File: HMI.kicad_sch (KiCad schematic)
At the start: 1 part, among them U8 XIAO-RP2350-SMD

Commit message: many changes
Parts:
- added C12, C40, C41, C42, C43, C44: 470n, Capacitor_SMD:C_1210_3225Metric_Pad1.33x2.70mm_HandSolder, symbol Device:C
- added C15, C16, C19, C20, C21, C22, C25, C26: 100n, Capacitor_SMD:C_1210_3225Metric_Pad1.33x2.70mm_HandSolder, symbol Device:C
- added C23, C24: 22p, Capacitor_SMD:C_1210_3225Metric_Pad1.33x2.70mm_HandSolder, symbol Device:C
- added D21, D22: LED, LED_SMD:LED_1210_3225Metric_Pad1.42x2.65mm_HandSolder, symbol Device:LED
- added J2: Conn_01x04, I2C OLED:I2C OLED, symbol Connector_Generic:Conn_01x04
- added J3: Conn_01x06, Connector_JST:JST_PH_B6B-PH-K_1x06_P2.00mm_Vertical, symbol Connector_Generic:Conn_01x06
- added LED1, LED2, LED3, LED4, LED5, LED6: SK6812MINI-E, PCM_marbastlib-various:LED_6028R, symbol PCM_marbastlib-various:SK6812MINI-E
- added MX1, MX2, MX3, MX4, MX5, MX6: MX_SW_solder, PCM_marbastlib-mx:SW_MX_1u, symbol PCM_marbastlib-mx:MX_SW_solder
- added R16, R17, R18, R23, R24, R25, R26, R27, R28, R29, R30, R31, R32, R33, R34, R35, R36, R37, R44, R8, R9: 10k, Resistor_SMD:R_1210_3225Metric_Pad1.30x2.65mm_HandSolder, symbol Device:R
- added R38, R39: 5.1k, Resistor_SMD:R_1210_3225Metric_Pad1.30x2.65mm_HandSolder, symbol Device:R
- added R40, R41, R42, R43, R45: 330, Resistor_SMD:R_1210_3225Metric_Pad1.30x2.65mm_HandSolder, symbol Device:R
- added RV4, RV5, RV6, RV7: 10k, Potentiometer_THT:Potentiometer_Bourns_3299W_Vertical, symbol Device:R_Potentiometer_Trim
- added SW1, SW2: RotaryEncoder_Switch, Rotary_Encoder:RotaryEncoder_Alps_EC11E-Switch_Vertical_H20mm, symbol Device:RotaryEncoder_Switch
- added TP4: SDA0, TestPoint:TestPoint_Keystone_5019_Miniature, symbol Connector:TestPoint
- added TP5: SCL0, TestPoint:TestPoint_Keystone_5019_Miniature, symbol Connector:TestPoint
- added TP6: SDA1, TestPoint:TestPoint_Keystone_5019_Miniature, symbol Connector:TestPoint
- added TP7: SCL1, TestPoint:TestPoint_Keystone_5019_Miniature, symbol Connector:TestPoint
- added U10: 74AHC1G14, symbol 74xGxx:74AHC1G14
- added U11: CH340G, Package_SO:SOIC-16_3.9x9.9mm_P1.27mm, symbol Interface_USB:CH340G
- added U12, U9: Optocoupler_DC_PhotoNPN_AKEC, Package_DIP:DIP-4_W7.62mm_Socket_LongPads, symbol Isolator:Optocoupler_DC_PhotoNPN_AKEC
- added U6: MCP23018x-x-SO, Package_SO:SOIC-28W_7.5x17.9mm_P1.27mm, symbol Interface_Expansion:MCP23018x-x-SO
- added Y1: 12MHz, Crystal:Crystal_SMD_3225-4Pin_3.2x2.5mm, symbol Device:Crystal_GND24
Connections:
- net +5V: now also U10.5 (VCC)
- net GND: now also C12.2, C15.2, C16.2, C19.2, C20.2, C21.2, C22.2, C40.2, C41.2, C42.2, C43.2, C44.2, J2.1 (Pin_1), LED1.4 (VSS), LED2.4 (VSS), LED3.4 (VSS), LED4.4 (VSS), LED5.4 (VSS), LED6.4 (VSS), R9.1, SW1.C, SW1.S2, SW2.C, SW2.S2, U10.3 (GND), U12.2, U6.1 (V_{SS}), U9.3
- net CV_{thermal}: now reaches U8.1 (GPIO26/D0/ADC0)
- net OE: now reaches U8.10 (GPIO4/D9/SPI0_MISO)
- net SPI: now reaches U8.11 (GPIO3/D10/SPI0_MOSI)
- net SPI: now also R45.1
- net +3V3: now reaches U8.12 (3V3)
- net +3V3: now also MX1.1, MX2.1, MX3.1, MX4.1, MX5.1, MX6.1, R18.2, R23.2, R24.2, R28.2, R29.2, R30.2, R44.2, R8.1, RV4.2, RV4.3, RV5.2, RV5.3, RV6.2, RV6.3, RV7.2, RV7.3, U6.11 (V_{DD})
- net RXD: now reaches U8.15 (GPIO21/D11/RX1)
- net RXD: now also R41.1, R44.1
- net TXD: now reaches U8.16 (GPIO20/D12/TX1)
- net TXD: now also R40.1
- net CC_{thermal}: now reaches U8.2 (GPIO27/D1/ADC1)
- net SDA1: now reaches U8.5 (GPIO6/D4/SDA1)
- net SDA1: now also J2.4 (Pin_4), RV6.1, TP6.1, U6.13 (SDA)
- net SCL1: now reaches U8.6 (GPIO7/D5/SCL1)
- net SCL1: now also J2.3 (Pin_3), RV7.1, TP7.1, U6.12 (SCL)
- net muxIntA: now reaches U8.8 (GPIO1/D7/RX0)
- net muxIntA: now also U6.19 (INTA)
- net muxIntB: now reaches U8.9 (GPIO2/D8/SPI0_SCK)
- net muxIntB: now also U6.18 (INTB)
- net SCL renamed SCL0
- net SCL0: now also RV5.1, TP5.1
- net SDA renamed SDA0
- net SDA0: now also RV4.1, TP4.1
- new net: MX1.2, R32.1
- new net: MX2.2, R33.1
- new net: R16.2, R23.1, SW1.B
- new net: MX6.2, R37.1
- new net: D22.1 (K), U12.4
- new net: LED2.2 (DOUT), LED3.3 (DIN)
- new net: LED1.2 (DOUT), LED2.3 (DIN)
- new net: R26.2, R28.1, SW2.A
- new net: R30.1, R31.1, SW2.S1
- new net: LED5.2 (DOUT), LED6.3 (DIN)
- new net: LED4.2 (DOUT), LED5.3 (DIN)
- new net: LED1.3 (DIN), U10.4
- new net: R27.2, R29.1, SW2.B
- new net: R17.2, R18.1, SW1.A
- new net: C25.1, U11.4 (V3)
- new net: MX3.2, R34.1
- new net: R24.1, R25.1, SW1.S1
- new net: MX4.2, R35.1
- new net: R9.2, U6.15 (ADDR)
- new net: R8.2, U6.16 (~{RESET})
- new net: MX5.2, R36.1
- new net: R41.2, U9.4
- new net: R45.2, U10.2
- new net: D21.1 (K), U9.1
- new net: R43.1, U9.2
- new net: LED3.2 (DOUT), LED4.3 (DIN)
- new net: R43.2, U11.2 (TXD)
- new net: R42.2, U11.3 (RXD)
- new net: C23.2, U11.7 (XI), Y1.3
- new net: C24.2, U11.8 (XO), Y1.1
- new net: R40.2, U12.1
- new net: R42.1, U12.3
- new net CC1: J3.2 (Pin_2), R39.2
- new net CC2: J3.3 (Pin_3), R38.2
- new net GNDD: C23.1, C24.1, C25.2, C26.2, J3.6 (Pin_6), R38.1, R39.1, U11.1 (GND), Y1.2 (G), Y1.4 (G)
- new net UD+: J3.4 (Pin_4), U11.5 (UD+)
- new net UD-: J3.5 (Pin_5), U11.6 (UD-)
- new net VUSB: C26.1, D21.2 (A), D22.2 (A), J3.1 (Pin_1), U11.16 (VCC)
- new net V_{OUT}+5V: J2.2 (Pin_2), LED1.1 (VDD), LED2.1 (VDD), LED3.1 (VDD), LED4.1 (VDD), LED5.1 (VDD), LED6.1 (VDD)
- new net btnCC: C41.1, R36.2, U6.7 (GPB4)
- new net btnCV: C12.1, R35.2, U6.6 (GPB3)
- new net btnCancel: C42.1, R32.2, U6.3 (GPB0)
- new net btnI_{lim}: C43.1, R34.2, U6.5 (GPB2)
- new net btnOE: C44.1, R37.2, U6.8 (GPB5)
- new net btnV_{lim}: C40.1, R33.2, U6.4 (GPB1)
- new net encLimA: C20.1, R26.1, U6.23 (GPA3)
- new net encLimB: C21.1, R27.1, U6.24 (GPA4)
- new net encLimS: C22.1, R31.2, U6.25 (GPA5)
- new net encSetA: C16.1, R17.1, U6.20 (GPA0)
- new net encSetB: C15.1, R16.1, U6.21 (GPA1)
- new net encSetS: C19.1, R25.2, U6.22 (GPA2)
- no-connect marks 0 -> 26
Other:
- note added: "12.345"
- note added: "CV"
- note added: "ENC_{lim}"
- note added: "ENC_{set}"
- note added: "GPIO expander"
- note added: "I2C0 for PSU monitoring + control"
- note added: "I2C1 for HMI"
- note added: "Key backlighting"
- note added: "Meas 12.345 A"
- note added: "Rotary encoders + debouncing"
- note added: "SP 12.345 V"
- note added: "To I2C Display"
- note added: "USB -> UART + optical isolation"
- note added: "btn CV btn CC"
- note added: "btn Cancel"
- note added: "btn I_{lim}"
- note added: "btn OE"
- note added: "btn V_{lim}"
- moved on the sheet: U8

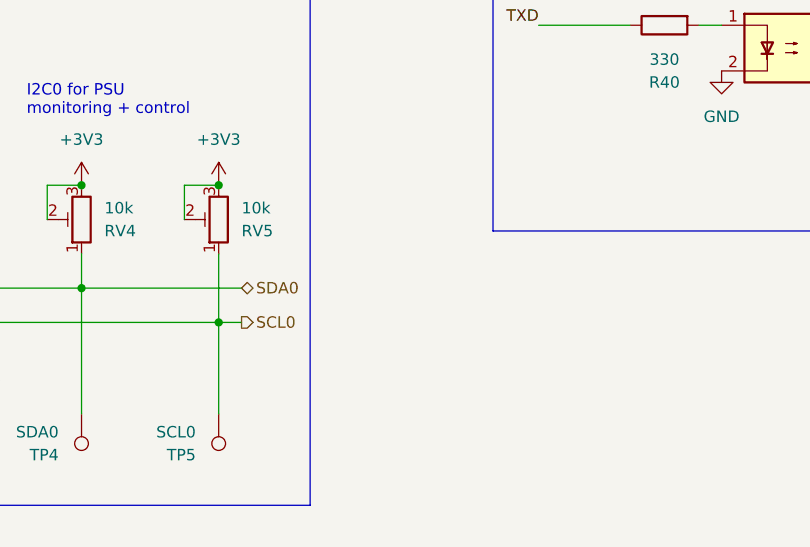
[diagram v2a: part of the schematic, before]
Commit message: shrink regulator board a little
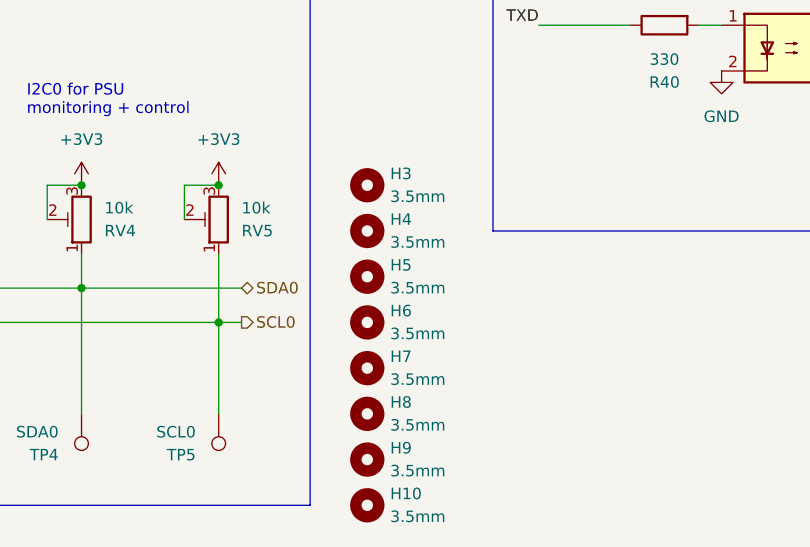
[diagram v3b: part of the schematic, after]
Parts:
- added H10, H3, H4, H5, H6, H7, H8, H9: 3.5mm, MountingHole:MountingHole_3mm_Pad, symbol Mechanical:MountingHole

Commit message: kicad v10. many changes to invididual boards
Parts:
- added C45: 100n, Capacitor_SMD:C_1210_3225Metric_Pad1.33x2.70mm_HandSolder, symbol Device:C
- LED1, LED2, LED3, LED4, LED5, LED6: footprint PCM_marbastlib-various:LED_6028R -> PCM_marbastlib-mx:LED_MX_6028R
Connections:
- net +3V3: now also J2.2 (Pin_2), R18.1, R23.1, R24.1, R8.2, C45.2; no longer R18.2, R23.2, R24.2, R8.1
- net +5V: no longer U8.14 (5V)
- net GND: now also C15.1, C16.1, C19.1, C40.1, C42.1, C43.1, R9.2, C45.1; no longer C15.2, C16.2, C19.2, C40.2, C42.2, C43.2, R9.1
- net V_{OUT}+5V: no longer J2.2 (Pin_2)
- net btnCC: now also R36.1; no longer R36.2
- net btnCV: now also R35.1; no longer R35.2
- net btnCancel: now also C42.2, U6.5 (GPB2); no longer C42.1, U6.3 (GPB0)
- net btnI_{lim}: now also C43.2, U6.4 (GPB1); no longer C43.1, U6.5 (GPB2)
- net btnOE: now also R37.1; no longer R37.2
- net btnV_{lim}: now also C40.2, U6.3 (GPB0); no longer C40.1, U6.4 (GPB1)
- net encSetA: now also C16.2, R17.2; no longer C16.1, R17.1
- net encSetB: now also C15.2, R16.2; no longer C15.1, R16.1
- net encSetS: now also C19.2; no longer C19.1
- net at MX6.2: now also R37.2; no longer R37.1
- net at R25.1, SW1.S1: now also R24.2; no longer R24.1
- net at MX4.2: now also R35.2; no longer R35.1
- net at U6.15 (ADDR): now also R9.1; no longer R9.2
- net at U6.16 (~{RESET}): now also R8.1; no longer R8.2
- net at MX5.2: now also R36.2; no longer R36.1
- new net: R16.1, R23.2, SW1.B
- new net: R17.1, R18.2, SW1.A
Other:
- moved on the sheet: C15, C19, R16, R17, R18, R35, R36, R37, R8, R9

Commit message: interim commit
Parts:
- removed H5, H6: 3.5mm, MountingHole:MountingHole_3mm_Pad, symbol Mechanical:MountingHole
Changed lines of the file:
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@@
 	)
 	(symbol
-		(lib_id "Mechanical:MountingHole")
-		(at 146.05 170.18 0)
-		(unit 1)
-		(body_style 1)
-		(exclude_from_sim no)
-		(in_bom no)
-		(on_board yes)
-		(in_pos_files yes)
-		(dnp no)
-		(fields_autoplaced yes)
-		(property "Reference" "H5"
-			(at 148.59 168.9099 0)
-			(show_name no)
-			(do_not_autoplace no)
-			(effects
-				(font
-					(size 1.27 1.27)
-				)
-				(justify left)
-			)
-		)
-		(property "Value" "3.5mm"
-			(at 148.59 171.4499 0)
-			(show_name no)
-			(do_not_autoplace no)
-			(effects
-				(font
-					(size 1.27 1.27)
-				)
-				(justify left)
-			)
-		)
-		(property "Footprint" "MountingHole:MountingHole_3mm_Pad"
-			(at 146.05 170.18 0)
-			(hide yes)
-			(show_name no)
-			(do_not_autoplace no)
-			(effects
-				(font
-					(size 1.27 1.27)
-				)
-			)
-		)
-		(property "Datasheet" ""
-			(at 146.05 170.18 0)
-			(hide yes)
-			(show_name no)
-			(do_not_autoplace no)
-			(effects
-				(font
-					(size 1.27 1.27)
-				)
-			)
-		)
-		(property "Description" "Mounting Hole without connection"
-			(at 146.05 170.18 0)
-			(hide yes)
-			(show_name no)
-			(do_not_autoplace no)
-			(effects
-				(font
-					(size 1.27 1.27)
-				)
-			)
-		)
-		(instances
-			(project "Lab PSU"
-				(path "/fae13b61-4b38-45f0-834d-dde0b60d6e74/df4c2f50-cbb9-473b-9738-1671ff8649a0"
-					(reference "H5")
-					(unit 1)
-				)
-			)
-		)
-	)
-	(symbol
 		(lib_id "power:+5V")
 		(at 134.62 25.4 0)
@@
 					(unit 1)
 				)
-			)
-		)
-	)
-	(symbol
-		(lib_id "Mechanical:MountingHole")
-		(at 146.05 175.26 0)
-		(unit 1)
-		(body_style 1)
-		(exclude_from_sim no)
-		(in_bom no)
-		(on_board yes)
-		(in_pos_files yes)
-		(dnp no)
-		(fields_autoplaced yes)
-		(property "Reference" "H6"
-			(at 148.59 173.9899 0)
-			(show_name no)
-			(do_not_autoplace no)
-			(effects
-				(font
-					(size 1.27 1.27)
-				)
-				(justify left)
-			)
-		)
-		(property "Value" "3.5mm"
-			(at 148.59 176.5299 0)
-			(show_name no)
-			(do_not_autoplace no)
-			(effects
-				(font
-					(size 1.27 1.27)
-				)
-				(justify left)
-			)
-		)
-		(property "Footprint" "MountingHole:MountingHole_3mm_Pad"
-			(at 146.05 175.26 0)
-			(hide yes)
-			(show_name no)
-			(do_not_autoplace no)
-			(effects
-				(font
-					(size 1.27 1.27)
-				)
-			)
-		)
-		(property "Datasheet" ""
-			(at 146.05 175.26 0)
-			(hide yes)
-			(show_name no)
-			(do_not_autoplace no)
-			(effects
-				(font
-					(size 1.27 1.27)
-				)
-			)
-		)
-		(property "Description" "Mounting Hole without connection"
-			(at 146.05 175.26 0)
-			(hide yes)
-			(show_name no)
-			(do_not_autoplace no)
-			(effects
-				(font
-					(size 1.27 1.27)
-				)
-			)
-		)
-		(instances
-			(project "Lab PSU"
-				(path "/fae13b61-4b38-45f0-834d-dde0b60d6e74/df4c2f50-cbb9-473b-9738-1671ff8649a0"
-					(reference "H6")
-					(unit 1)
-				)
